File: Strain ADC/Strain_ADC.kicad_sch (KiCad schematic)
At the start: 76 parts, among them J11 Conn_01x05, U1 MCP3421A0T-ECH, U2 MCP3421A0T-ECH, U3 MCP3421A0T-ECH, U4 MCP3421A0T-ECH, U5 MCP3421A0T-ECH, U6 TCA9548APWR, U7 ADC081C021CIMM

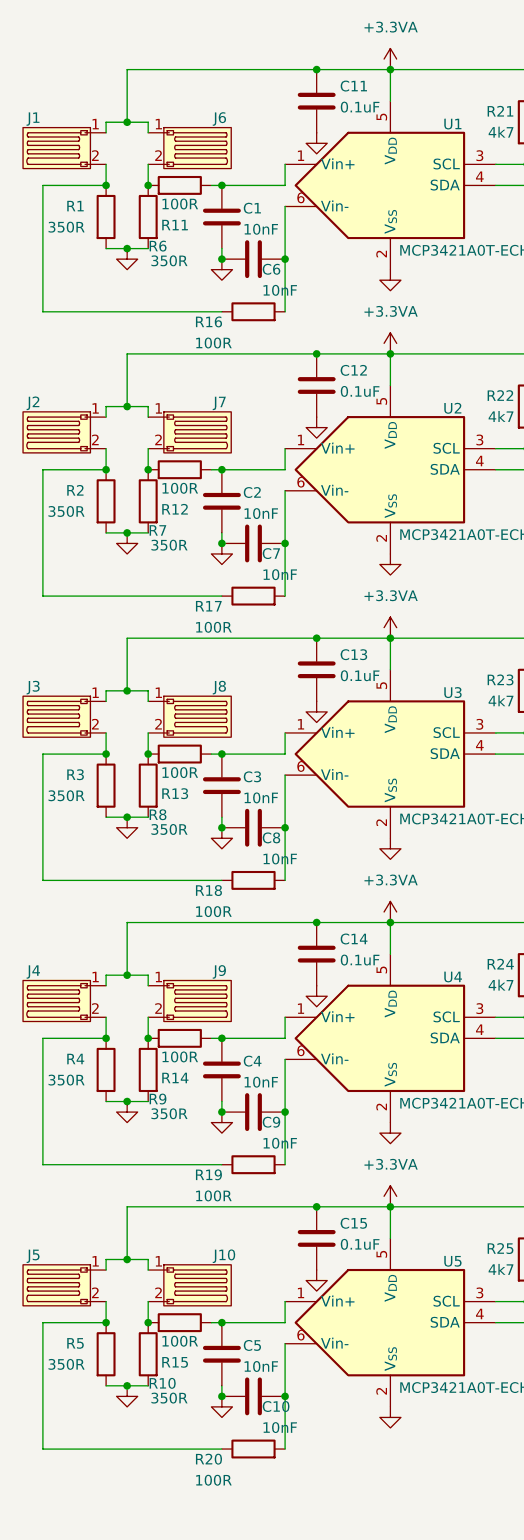
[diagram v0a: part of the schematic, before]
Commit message: Add part numbers to remaining PCBs, change part numbers on sensor board, redo strain adc layout
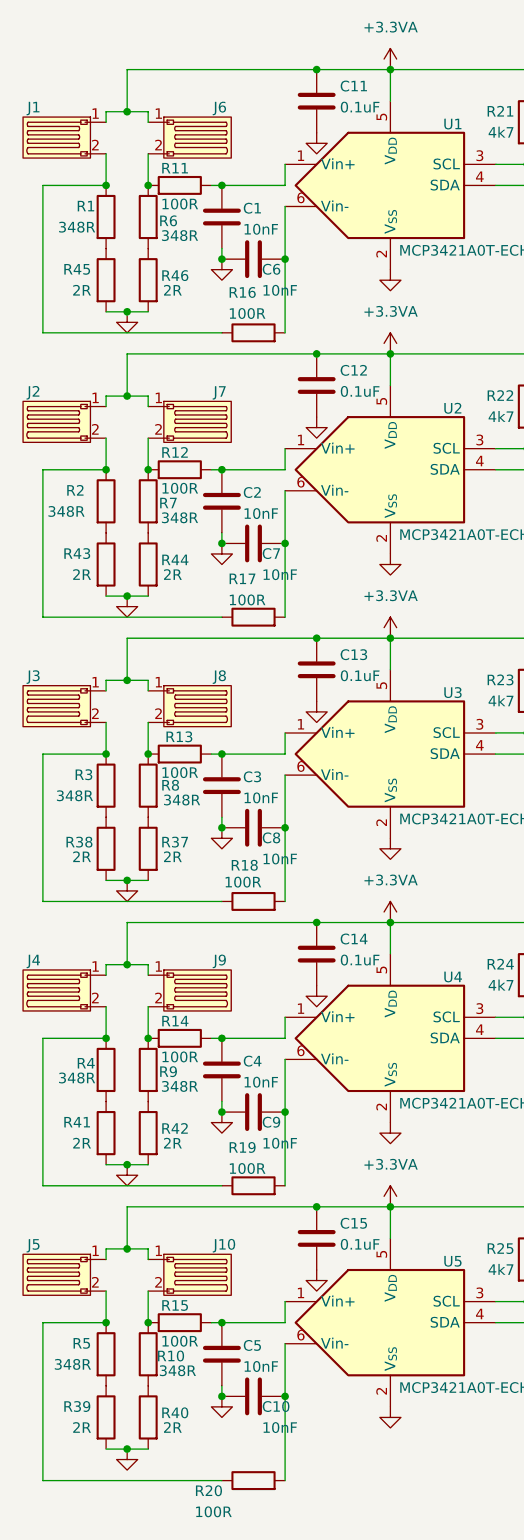
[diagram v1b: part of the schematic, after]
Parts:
- added R37, R38, R39, R40, R41, R42, R43, R44, R45, R46: 2R, Resistor_SMD:R_0603_1608Metric, symbol Device:R
- C1, C10, C2, C3, C4, C5, C6, C7, C8, C9: Part Number (none) -> GRM155R71C103KA01D
- C11, C12, C13, C14, C15, C16, C17: Part Number (none) -> CL05B104KP5NNNC
- C18, C20: Part Number (none) -> CL05A106MQ5NUNC
- C19: Part Number (none) -> GRM155R70J105KA12D
- J11: Part Number (none) -> B5B-XH-A
- R1, R10, R2, R3, R4, R5, R6, R7, R8, R9: value 350R -> 348R; Part Number (none) -> ERA-2AEB3480X
- R11, R12, R13, R14, R15, R16, R17, R18, R19, R20: Part Number (none) -> CRCW0402100RFKEDC
- R21, R22, R23, R24, R25, R26, R27, R28, R29, R30, R31, R32: Part Number (none) -> RC0402FR-074K7L
- R33, R34: Part Number (none) -> RC0402FR-072K2L
- R35: Part Number (none) -> ERJ-2RKF5102X
- R36: Part Number (none) -> RC0402JR-0710KL
- U1, U2, U3, U4, U5: Part Number (none) -> MCP3421A0T-E/CH
- U6: Part Number (none) -> TCA9548APWR
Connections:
- net GND: now also R37.2, R38.2, R39.2, R40.2, R41.2, R42.2, R43.2, R44.2, R45.2, R46.2; no longer R1.2, R10.2, R2.2, R3.2, R4.2, R5.2, R6.2, R7.2, R8.2, R9.2
- new net: R10.2, R40.1
- new net: R46.1, R6.2
- new net: R4.2, R41.1
- new net: R44.1, R7.2
- new net: R42.1, R9.2
- new net: R1.2, R45.1
- new net: R39.1, R5.2
- new net: R2.2, R43.1
- new net: R3.2, R38.1
- new net: R37.1, R8.2
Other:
- moved on the sheet: J1, J10, J2, J3, J4, J5, J6, J7, J8, J9, R16, R17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
